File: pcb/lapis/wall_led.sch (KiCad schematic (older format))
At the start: 0 parts

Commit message: 基板修正途中　ソフト動作確認まで
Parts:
- added C5: 0.1u, Capacitor_SMD:C_0201_0603Metric_Pad0.64x0.40mm_HandSolder, symbol Device:C
- added D1, D2: OSI5FU3A11C, LED_THT:LED_D3.0mm_Horizontal_O1.27mm_Z2.0mm_IRBlack, symbol Device:LED
- added R1: 1, Resistor_SMD:R_0201_0603Metric_Pad0.64x0.40mm_HandSolder, symbol Device:R
- added U3: NJU6080, Package_TO_SOT_SMD:SOT-23-6, symbol lapis-rescue:NJU6080-NJU6080
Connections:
- new net: R1.1, U3.3 (Rs)
- new net: D2.1 (K), U3.4 (LED)
- new net: D1.1 (K), D2.2 (A)
- new net +3V3: C5.1, U3.5 (EN), U3.6 (VDD)
- new net +BATT: D1.2 (A)
- new net GND: C5.2, R1.2, U3.2 (GND)
- new net LED_PWM: U3.1 (PWM)
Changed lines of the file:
@@
 $Descr A4 11693 8268
 encoding utf-8
-Sheet 1 14
+Sheet 10 14
 Title ""
 Date ""
@@
 Comment4 ""
 $EndDescr
+$Comp
+L lapis-rescue:NJU6080-NJU6080 U3
+U 1 1 5FB6344A
+P 5950 3750
+AR Path="/5FA82034/5FB6344A" Ref="U3"  Part="1"
+AR Path="/5FA82132/5FB6344A" Ref="U4"  Part="1"
+F 0 "U4" H 5950 3765 50  0000 C CNN
+F 1 "NJU6080" H 5950 3674 50  0000 C CNN
+F 2 "Package_TO_SOT_SMD:SOT-23-6" H 5950 3750 50  0001 C CNN
+F 3 "" H 5950 3750 50  0001 C CNN
+	1    5950 3750
+	1    0    0    -1
+$EndComp
+$Comp
+L Device:LED D1
+U 1 1 5FB63D26
+P 6800 3650
+AR Path="/5FA82034/5FB63D26" Ref="D1"  Part="1"
+AR Path="/5FA82132/5FB63D26" Ref="D4"  Part="1"
+F 0 "D4" V 6839 3532 50  0000 R CNN
+F 1 "OSI5FU3A11C" V 6748 3532 50  0000 R CNN
+F 2 "LED_THT:LED_D3.0mm_Horizontal_O1.27mm_Z2.0mm_IRBlack" H 6800 3650 50  0001 C CNN
+F 3 "~" H 6800 3650 50  0001 C CNN
+	1    6800 3650
+	0    -1   -1   0
+$EndComp
+$Comp
+L Device:LED D2
+U 1 1 5FB64371
+P 6800 4100
+AR Path="/5FA82034/5FB64371" Ref="D2"  Part="1"
+AR Path="/5FA82132/5FB64371" Ref="D5"  Part="1"
+F 0 "D5" V 6839 3982 50  0000 R CNN
+F 1 "OSI5FU3A11C" V 6748 3982 50  0000 R CNN
+F 2 "LED_THT:LED_D3.0mm_Horizontal_O1.27mm_Z2.0mm_IRBlack" H 6800 4100 50  0001 C CNN
+F 3 "~" H 6800 4100 50  0001 C CNN
+	1    6800 4100
+	0    -1   -1   0
+$EndComp
+$Comp
+L power:+3.3V #PWR0110
+U 1 1 5FB658FD
+P 6500 3350
+AR Path="/5FA82034/5FB658FD" Ref="#PWR0110"  Part="1"
+AR Path="/5FA82132/5FB658FD" Ref="#PWR0155"  Part="1"
+F 0 "#PWR0155" H 6500 3200 50  0001 C CNN
+F 1 "+3.3V" H 6515 3523 50  0000 C CNN
+F 2 "" H 6500 3350 50  0001 C CNN
+F 3 "" H 6500 3350 50  0001 C CNN
+	1    6500 3350
+	1    0    0    -1
+$EndComp
+$Comp
+L power:GND #PWR0111
+U 1 1 5FB661D5
+P 5350 4950
+AR Path="/5FA82034/5FB661D5" Ref="#PWR0111"  Part="1"
+AR Path="/5FA82132/5FB661D5" Ref="#PWR0156"  Part="1"
+F 0 "#PWR0156" H 5350 4700 50  0001 C CNN
+F 1 "GND" H 5355 4777 50  0000 C CNN
+F 2 "" H 5350 4950 50  0001 C CNN
+F 3 "" H 5350 4950 50  0001 C CNN
+	1    5350 4950
+	1    0    0    -1
+$EndComp
+$Comp
+L Device:R R1
+U 1 1 5FB665AB
+P 5500 4550
+AR Path="/5FA82034/5FB665AB" Ref="R1"  Part="1"
+AR Path="/5FA82132/5FB665AB" Ref="R10"  Part="1"
+F 0 "R10" H 5570 4596 50  0000 L CNN
+F 1 "1" H 5570 4505 50  0000 L CNN
+F 2 "Resistor_SMD:R_0201_0603Metric_Pad0.64x0.40mm_HandSolder" V 5430 4550 50  0001 C CNN
+F 3 "~" H 5500 4550 50  0001 C CNN
+	1    5500 4550
+	1    0    0    -1
+$EndComp
+Wire Wire Line
+	6800 3350 6800 3500
+Wire Wire Line
+	6800 3800 6800 3950
+Wire Wire Line
+	6800 4300 6300 4300
+Wire Wire Line
+	6800 4250 6800 4300
+Wire Wire Line
+	6500 3350 6500 4000
+Wire Wire Line
+	6500 4150 6300 4150
+Wire Wire Line
+	6300 4000 6500 4000
+Connection ~ 6500 4000
+Wire Wire Line
+	6500 4000 6500 4150
+Wire Wire Line
+	5500 4300 5500 4400
+Wire Wire Line
+	5600 4300 5500 4300
+Wire Wire Line
+	5600 4150 5350 4150
+Wire Wire Line
+	5350 4150 5350 4800
+Wire Wire Line
+	5500 4800 5350 4800
+Connection ~ 5350 4800
+Wire Wire Line
+	5350 4800 5350 4950
+Wire Wire Line
+	5500 4700 5500 4800
+Wire Wire Line
+	5500 4000 5600 4000
+Text HLabel 5500 4000 0    50   Input ~ 0
+LED_PWM
+$Comp
+L power:+3.3V #PWR0112
+U 1 1 5FB69D30
+P 4200 3700
+AR Path="/5FA82034/5FB69D30" Ref="#PWR0112"  Part="1"
+AR Path="/5FA82132/5FB69D30" Ref="#PWR0157"  Part="1"
+F 0 "#PWR0157" H 4200 3550 50  0001 C CNN
+F 1 "+3.3V" H 4215 3873 50  0000 C CNN
+F 2 "" H 4200 3700 50  0001 C CNN
+F 3 "" H 4200 3700 50  0001 C CNN
+	1    4200 3700
+	1    0    0    -1
+$EndComp
+$Comp
+L Device:C C5
+U 1 1 5FB69FDF
+P 4200 4050
+AR Path="/5FA82034/5FB69FDF" Ref="C5"  Part="1"
+AR Path="/5FA82132/5FB69FDF" Ref="C22"  Part="1"
+F 0 "C22" H 4315 4096 50  0000 L CNN
+F 1 "0.1u" H 4315 4005 50  0000 L CNN
+F 2 "Capacitor_SMD:C_0201_0603Metric_Pad0.64x0.40mm_HandSolder" H 4238 3900 50  0001 C CNN
+F 3 "~" H 4200 4050 50  0001 C CNN
+	1    4200 4050
+	1    0    0    -1
+$EndComp
+$Comp
+L power:GND #PWR0113
+U 1 1 5FB6A85A
+P 4200 4400
+AR Path="/5FA82034/5FB6A85A" Ref="#PWR0113"  Part="1"
+AR Path="/5FA82132/5FB6A85A" Ref="#PWR0158"  Part="1"
+F 0 "#PWR0158" H 4200 4150 50  0001 C CNN
+F 1 "GND" H 4205 4227 50  0000 C CNN
+F 2 "" H 4200 4400 50  0001 C CNN
+F 3 "" H 4200 4400 50  0001 C CNN
+	1    4200 4400
+	1    0    0    -1
+$EndComp
+Wire Wire Line
+	4200 3900 4200 3700
+Wire Wire Line
+	4200 4200 4200 4400
+$Comp
+L power:+BATT #PWR0109
+U 1 1 60D437EA
+P 6800 3350
+AR Path="/5FA82034/60D437EA" Ref="#PWR0109"  Part="1"
+AR Path="/5FA82132/60D437EA" Ref="#PWR0127"  Part="1"
+F 0 "#PWR0127" H 6800 3200 50  0001 C CNN
+F 1 "+BATT" H 6815 3523 50  0000 C CNN
+F 2 "" H 6800 3350 50  0001 C CNN
+F 3 "" H 6800 3350 50  0001 C CNN
+	1    6800 3350
+	1    0    0    -1
+$EndComp
 $EndSCHEMATC

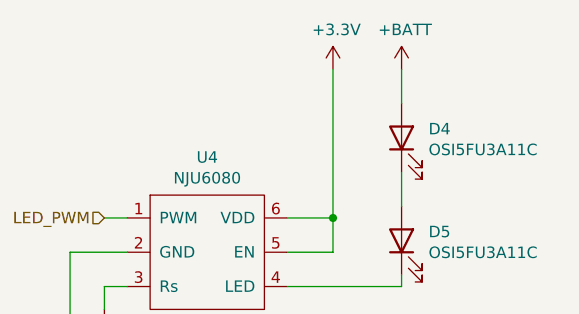
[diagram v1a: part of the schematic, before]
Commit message: STM411失敗基板　STM484に変更し基板修正
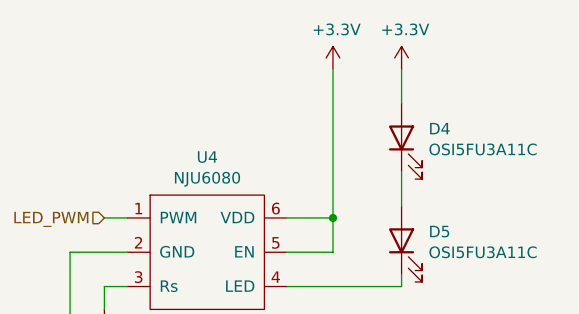
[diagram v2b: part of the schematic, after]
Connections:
- net +BATT is gone; now on net +3V3: D1.2 (A)
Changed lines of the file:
@@
 $EndComp
-Wire Wire Line
-	6800 3350 6800 3500
 Wire Wire Line
 	6800 3800 6800 3950
@@
 Wire Wire Line
 	4200 4200 4200 4400
+Wire Wire Line
+	6800 3350 6800 3500
 $Comp
-L power:+BATT #PWR0109
-U 1 1 60D437EA
+L power:+3.3V #PWR0109
+U 1 1 60DE475D
 P 6800 3350
-AR Path="/5FA82034/60D437EA" Ref="#PWR0109"  Part="1"
-AR Path="/5FA82132/60D437EA" Ref="#PWR0127"  Part="1"
+AR Path="/5FA82034/60DE475D" Ref="#PWR0109"  Part="1"
+AR Path="/5FA82132/60DE475D" Ref="#PWR0127"  Part="1"
 F 0 "#PWR0127" H 6800 3200 50  0001 C CNN
-F 1 "+BATT" H 6815 3523 50  0000 C CNN
+F 1 "+3.3V" H 6815 3523 50  0000 C CNN
 F 2 "" H 6800 3350 50  0001 C CNN
 F 3 "" H 6800 3350 50  0001 C CNN

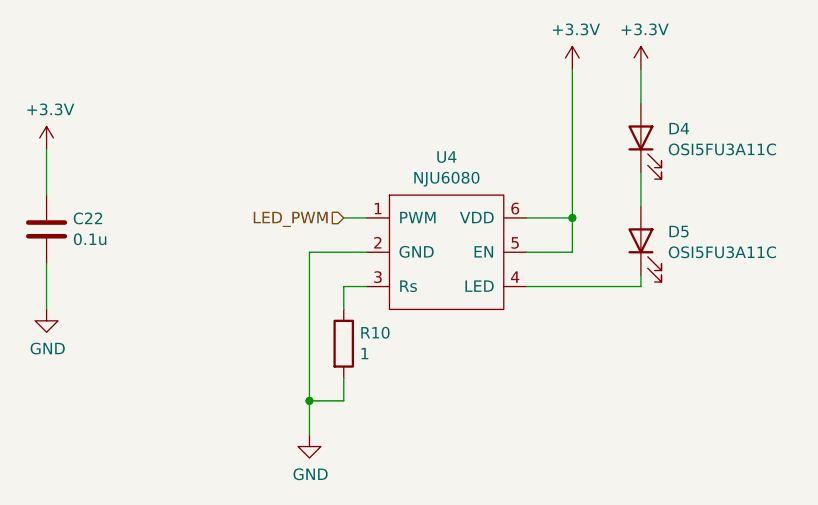
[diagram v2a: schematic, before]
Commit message: 信地旋回探索
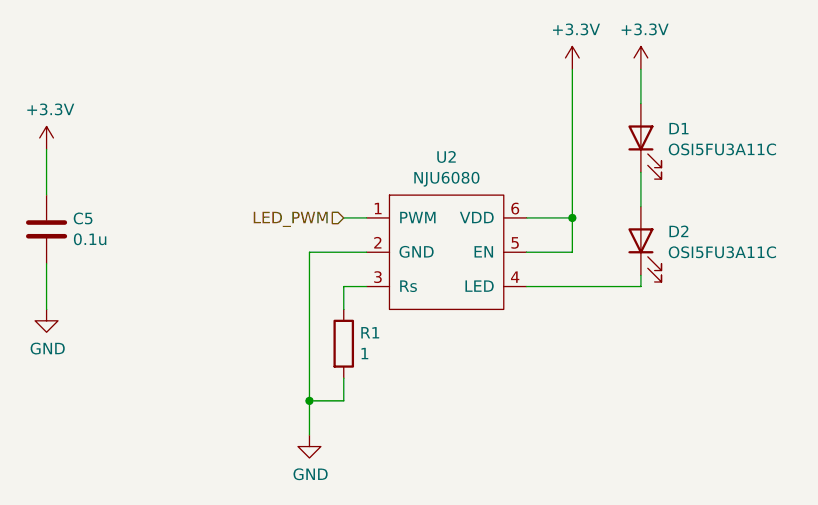
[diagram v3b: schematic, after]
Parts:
- renumbered U3 to U2
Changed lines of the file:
@@
 $Descr A4 11693 8268
 encoding utf-8
-Sheet 10 14
+Sheet 8 15
 Title ""
 Date ""
@@
 $EndDescr
 $Comp
-L lapis-rescue:NJU6080-NJU6080 U3
+L lapis-rescue:NJU6080-NJU6080 U2
 U 1 1 5FB6344A
 P 5950 3750
-AR Path="/5FA82034/5FB6344A" Ref="U3"  Part="1"
-AR Path="/5FA82132/5FB6344A" Ref="U4"  Part="1"
-F 0 "U4" H 5950 3765 50  0000 C CNN
+AR Path="/5FA82034/5FB6344A" Ref="U2"  Part="1"
+AR Path="/5FA82132/5FB6344A" Ref="U1"  Part="1"
+F 0 "U2" H 5950 3765 50  0000 C CNN
 F 1 "NJU6080" H 5950 3674 50  0000 C CNN
 F 2 "Package_TO_SOT_SMD:SOT-23-6" H 5950 3750 50  0001 C CNN
@@
 AR Path="/5FA82034/5FB63D26" Ref="D1"  Part="1"
 AR Path="/5FA82132/5FB63D26" Ref="D4"  Part="1"
-F 0 "D4" V 6839 3532 50  0000 R CNN
+F 0 "D1" V 6839 3532 50  0000 R CNN
 F 1 "OSI5FU3A11C" V 6748 3532 50  0000 R CNN
 F 2 "LED_THT:LED_D3.0mm_Horizontal_O1.27mm_Z2.0mm_IRBlack" H 6800 3650 50  0001 C CNN
@@
 AR Path="/5FA82034/5FB64371" Ref="D2"  Part="1"
 AR Path="/5FA82132/5FB64371" Ref="D5"  Part="1"
-F 0 "D5" V 6839 3982 50  0000 R CNN
+F 0 "D2" V 6839 3982 50  0000 R CNN
 F 1 "OSI5FU3A11C" V 6748 3982 50  0000 R CNN
 F 2 "LED_THT:LED_D3.0mm_Horizontal_O1.27mm_Z2.0mm_IRBlack" H 6800 4100 50  0001 C CNN
@@
 AR Path="/5FA82034/5FB658FD" Ref="#PWR0110"  Part="1"
 AR Path="/5FA82132/5FB658FD" Ref="#PWR0155"  Part="1"
-F 0 "#PWR0155" H 6500 3200 50  0001 C CNN
+F 0 "#PWR0110" H 6500 3200 50  0001 C CNN
 F 1 "+3.3V" H 6515 3523 50  0000 C CNN
 F 2 "" H 6500 3350 50  0001 C CNN
@@
 AR Path="/5FA82034/5FB661D5" Ref="#PWR0111"  Part="1"
 AR Path="/5FA82132/5FB661D5" Ref="#PWR0156"  Part="1"
-F 0 "#PWR0156" H 5350 4700 50  0001 C CNN
+F 0 "#PWR0111" H 5350 4700 50  0001 C CNN
 F 1 "GND" H 5355 4777 50  0000 C CNN
 F 2 "" H 5350 4950 50  0001 C CNN
@@
 AR Path="/5FA82034/5FB665AB" Ref="R1"  Part="1"
 AR Path="/5FA82132/5FB665AB" Ref="R10"  Part="1"
-F 0 "R10" H 5570 4596 50  0000 L CNN
+F 0 "R1" H 5570 4596 50  0000 L CNN
 F 1 "1" H 5570 4505 50  0000 L CNN
 F 2 "Resistor_SMD:R_0201_0603Metric_Pad0.64x0.40mm_HandSolder" V 5430 4550 50  0001 C CNN
@@
 AR Path="/5FA82034/5FB69D30" Ref="#PWR0112"  Part="1"
 AR Path="/5FA82132/5FB69D30" Ref="#PWR0157"  Part="1"
-F 0 "#PWR0157" H 4200 3550 50  0001 C CNN
+F 0 "#PWR0112" H 4200 3550 50  0001 C CNN
 F 1 "+3.3V" H 4215 3873 50  0000 C CNN
 F 2 "" H 4200 3700 50  0001 C CNN
@@
 AR Path="/5FA82034/5FB69FDF" Ref="C5"  Part="1"
 AR Path="/5FA82132/5FB69FDF" Ref="C22"  Part="1"
-F 0 "C22" H 4315 4096 50  0000 L CNN
+F 0 "C5" H 4315 4096 50  0000 L CNN
 F 1 "0.1u" H 4315 4005 50  0000 L CNN
 F 2 "Capacitor_SMD:C_0201_0603Metric_Pad0.64x0.40mm_HandSolder" H 4238 3900 50  0001 C CNN
@@
 AR Path="/5FA82034/5FB6A85A" Ref="#PWR0113"  Part="1"
 AR Path="/5FA82132/5FB6A85A" Ref="#PWR0158"  Part="1"
-F 0 "#PWR0158" H 4200 4150 50  0001 C CNN
+F 0 "#PWR0113" H 4200 4150 50  0001 C CNN
 F 1 "GND" H 4205 4227 50  0000 C CNN
 F 2 "" H 4200 4400 50  0001 C CNN
@@
 AR Path="/5FA82034/60DE475D" Ref="#PWR0109"  Part="1"
 AR Path="/5FA82132/60DE475D" Ref="#PWR0127"  Part="1"
-F 0 "#PWR0127" H 6800 3200 50  0001 C CNN
+F 0 "#PWR0109" H 6800 3200 50  0001 C CNN
 F 1 "+3.3V" H 6815 3523 50  0000 C CNN
 F 2 "" H 6800 3350 50  0001 C CNN
